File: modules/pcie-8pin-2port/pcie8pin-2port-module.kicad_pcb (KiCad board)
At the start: 4 copper layers, 109.7 x 66 mm, 24 parts, among them J1 TO-HUB, J5 USB-C 2.0, SW1 BOOT, SW2 RESET, U1 ESP32-S3-MINI-1-N4R2, U10 INA238, U11 INA238, U2 TJA1462A, U3 LP5907MFX-3.3

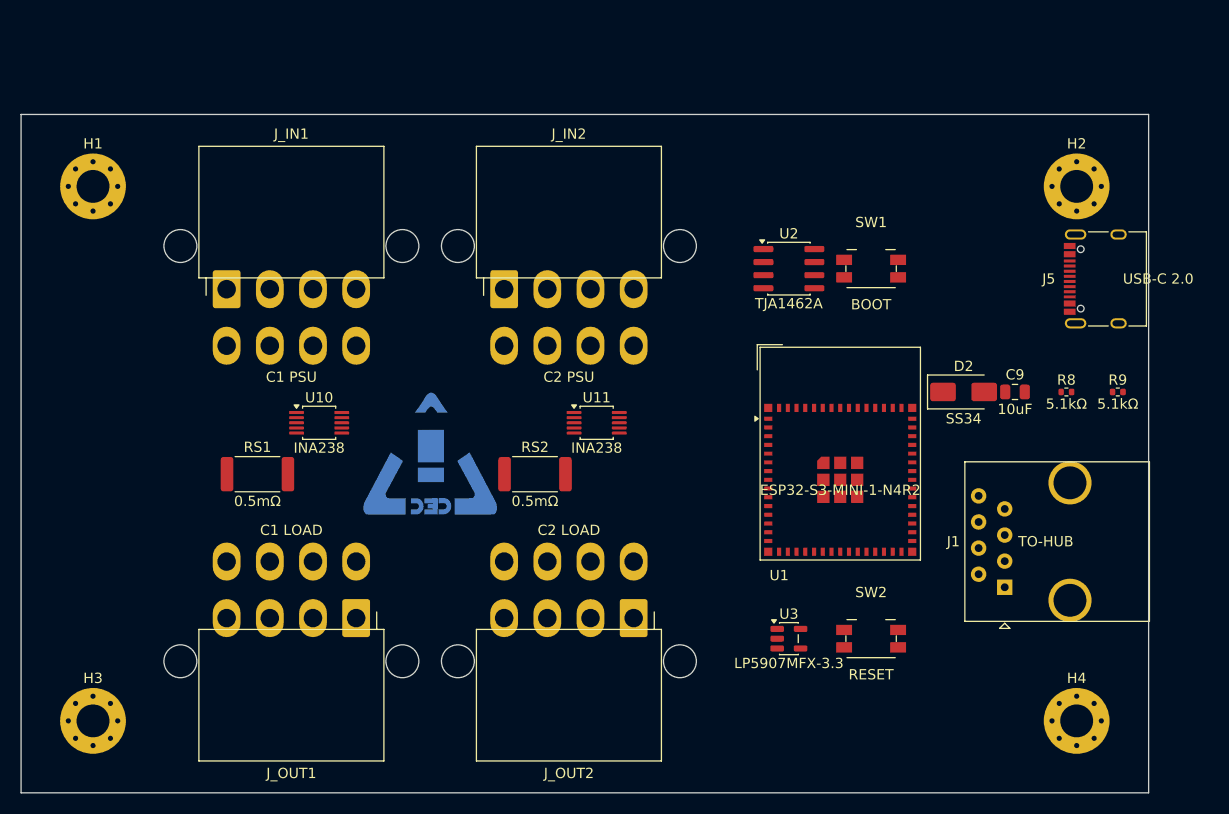
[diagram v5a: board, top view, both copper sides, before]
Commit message: pcie-2/3 PCB: condense + FTP jack (match the EPS pass)
Applied the same minimal-size / max-aggression pass to both PCIe SKUs, plus the
platform FTP jack swap.

- J1 RJ-45 -> platform FTP jack on both: footprint cec:RJ45_FTP_Shielded_Horizontal
  (Kinghelm KH-RJ45-58-8P8C, LCSC C2683360), SH1/SH2 -> GND (verbatim shield-tie
  splice; both PCIe J1 are at the same schematic position as the EPS/12VHPWR).
  Surgical edit (preserves the hand-applied sourcing); ERC benign-only, netlist
  verifies SH1/SH2 on GND + the FTP footprint. BOM CSVs J1 -> C2683360.
- Condensed PCB floorplans regenerated:
  - pcie-2port: 99 x 44 mm (identical geometry to the EPS, N=2): connectors
    overhang the edges, side-by-side sense band, RJ-45 mouth overhangs, USB-C on
    the top edge, 3 M3 mounts.
  - pcie-3port: 126 x 44 mm (N=3): same, but 5 M3 mounts -- the 3 base + two
    mid-height mounts in the inter-cable gaps so the long board doesn't flex (the
    overhang fills the top/bottom edges, leaving only the mid-height gaps free).
- gen-module-pcb.py: add inter-cable mid-height mounts for N>=3 cable boards.
- DRC 0 structural on both (only cosmetic silk + the benign lib_footprint_mismatch);
  renders confirm the FTP jack + the layout. PCBs still need GUI
  Update-from-Schematic + Fill Zones + route.

https://claude.ai/code/session_018vzBBqght166NSh7aJGKHf
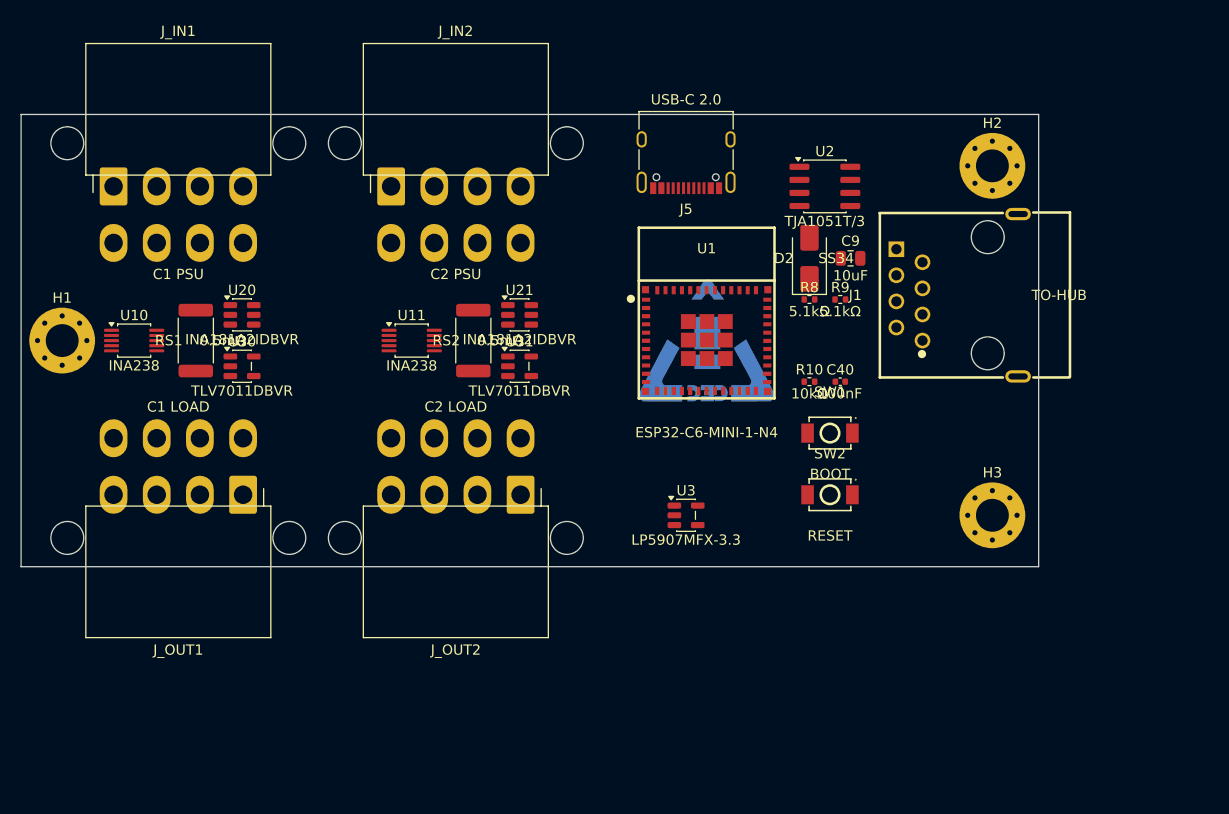
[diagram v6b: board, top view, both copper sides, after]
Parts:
- removed H4: MountingHole_3.2mm_M3_Pad_Via, cec-MountingHole:MountingHole_3.2mm_M3_Pad_Via
- added C40: 100nF, cec-Capacitor_SMD:C_0402_1005Metric, F.Cu at (79.7, 26.0)
- added R10: 10kΩ, cec-Resistor_SMD:R_0402_1005Metric, F.Cu at (76.7, 26.0)
- added U20: INA181A2IDBVR, cec-Package_TO_SOT_SMD:SOT-23-6, F.Cu at (21.5, 19.5)
- added U21: INA181A2IDBVR, cec-Package_TO_SOT_SMD:SOT-23-6, F.Cu at (48.5, 19.5)
- added U30: TLV7011DBVR, cec-Package_TO_SOT_SMD:SOT-23-5, F.Cu at (21.5, 24.5)
- added U31: TLV7011DBVR, cec-Package_TO_SOT_SMD:SOT-23-5, F.Cu at (48.5, 24.5)
- J1: footprint cec-Connector_RJ:RJ45_Amphenol_54602-x08_Horizontal -> cec:RJ45_FTP_Shielded_Horizontal
- SW1, SW2: footprint cec-Button_Switch_SMD:Panasonic_EVQPUJ_EVQPUA -> cec-Button_Switch_SMD:TS-1088-AR02016
- U1: value ESP32-S3-MINI-1-N4R2 -> ESP32-C6-MINI-1-N4; footprint cec-RF_Module:ESP32-S2-MINI-1_NoAntKeepout -> cec-RF_Module:ESP32-C6-MINI-1
- U2: value TJA1462A -> TJA1051T/3
- moved H3 89.8 mm to (94.5, 39.0)
- moved J5 42.9 mm to (64.7, 3.50), turned to 180 degrees
- moved LOGO1 29.1 mm to (66.7, 22.0)
- moved R9 28.5 mm to (79.7, 18.0)
- moved R8 26.6 mm to (76.7, 18.0)
- moved J1 25.3 mm to (87.7, 22.0)
- moved C9 20.6 mm to (80.7, 14.0)
- moved D2 19.8 mm to (76.7, 14.0), turned to 90 degrees
- moved U10 19.7 mm to (11.0, 22.0)
- moved U11 19.7 mm to (38.0, 22.0)
- moved U1 17.0 mm to (66.7, 22.0)
- moved SW1 16.5 mm to (78.7, 31.0)
- moved J_OUT1 16.3 mm to (21.6, 37.0)
- moved J_OUT2 16.3 mm to (48.6, 37.0)
- moved U3 15.6 mm to (64.7, 39.0)
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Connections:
- J1 pad SH1: unconnected-(J1-SHIELD-PadSH1) -> GND
- J1 pad SH2: unconnected-(J1-SHIELD-PadSH2) -> GND
- U1 pad 11: unconnected-(U1-IO7-Pad11) -> GND
- U1 pad 12: /I2C_SDA -> /DETECT_SENSE
- U1 pad 13: /I2C_SCL -> unconnected-(U1-IO1-Pad13)
- U1 pad 14: /DETECT_SENSE -> GND
- U1 pad 17: unconnected-(U1-IO13-Pad17) -> /USB_DM
- U1 pad 18: unconnected-(U1-IO14-Pad18) -> /USB_DP
- U1 pad 19: unconnected-(U1-IO15-Pad19) -> /THRESH_PWM
- U1 pad 21: /CAN_TX -> unconnected-(U1-NC-Pad21)
- U1 pad 22: /CAN_RX -> unconnected-(U1-IO8-Pad22)
- U1 pad 23: /USB_DM -> /GPIO0
- U1 pad 24: /USB_DP -> /I2C_SDA
- U1 pad 25: unconnected-(U1-IO21-Pad25) -> /I2C_SCL
- U1 pad 26: unconnected-(U1-IO26-Pad26) -> /CAN_TX
- U1 pad 27: unconnected-(U1-IO47-Pad27) -> /CAN_RX
- U1 pad 28: unconnected-(U1-IO33-Pad28) -> /DETC1
- U1 pad 29: unconnected-(U1-IO34-Pad29) -> /DETC2
- U1 pad 36: unconnected-(U1-IO40-Pad36) -> GND
- U1 pad 37: unconnected-(U1-IO41-Pad37) -> GND
- U1 pad 38: unconnected-(U1-IO42-Pad38) -> GND
- U1 pad 39: unconnected-(U1-TXD0-Pad39) -> GND
- U1 pad 4: /GPIO0 -> unconnected-(U1-NC-Pad4)
- U1 pad 40: unconnected-(U1-RXD0-Pad40) -> GND
- U1 pad 41: unconnected-(U1-IO45-Pad41) -> GND
- U1 pad 44: unconnected-(U1-IO46-Pad44) -> GND
- U1 pad 45: /EN -> GND
- U1 pad 8: unconnected-(U1-IO4-Pad8) -> /EN
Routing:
- added copper zone on In1.Cu, net GND
- added copper zone on In2.Cu, net GND
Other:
- board size 109.7 x 66 mm -> 99 x 44 mm

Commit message: Mini-Fit Jr footprint: correct pegs to the real Molex 5569-08A2 land
Verified the right-angle Mini-Fit Jr footprint against the actual Molex 5569-08A2
(KiCad-standard land / real drawing). The cec-derived land (made by trimming the
2x12 variant) had its two SNAP-IN PCB-lock pegs WRONG:

  was:  pegs (-4.5,-4.2) and (17.1,-4.2), 3.2mm drill  (outboard at the body ends)
  real: pegs (0,-7.3) and (12.6,-7.3),  3.0mm NPTH      (in line with the outer pins)

Signal pads (8x 2.7x3.7, 1.8mm, y0/5.5) and the F.Fab body already matched.
Also narrowed the courtyard to the real (-3.2,-14.4)..(15.8,7.85).

The real pegs sit ~3 mm further forward than the wrong ones, so the overhang
placement had to move the connectors inboard: gen-module-pcb.py JIN_Y 7 -> 10
(pegs now land 1.2 mm off the edge, mouth still overhangs ~3.9 mm), and the cable
boards grew H 44 -> 46 (BAND_Y 22 -> 23) to keep the side-by-side sense band clear
of the deeper connector courtyards.

PCIe-2 (99x46) and PCIe-3 (126x46) regenerated; DRC 0 structural, render confirms
the pegs now sit in line with the pins, on-board. EPS PCB intentionally NOT
regenerated (being hand-edited) -- it still carries the old peg land; on its next
Update-Footprints-from-Library the J_IN/J_OUT must shift to JIN_Y=10 / H=46.

https://claude.ai/code/session_018vzBBqght166NSh7aJGKHf
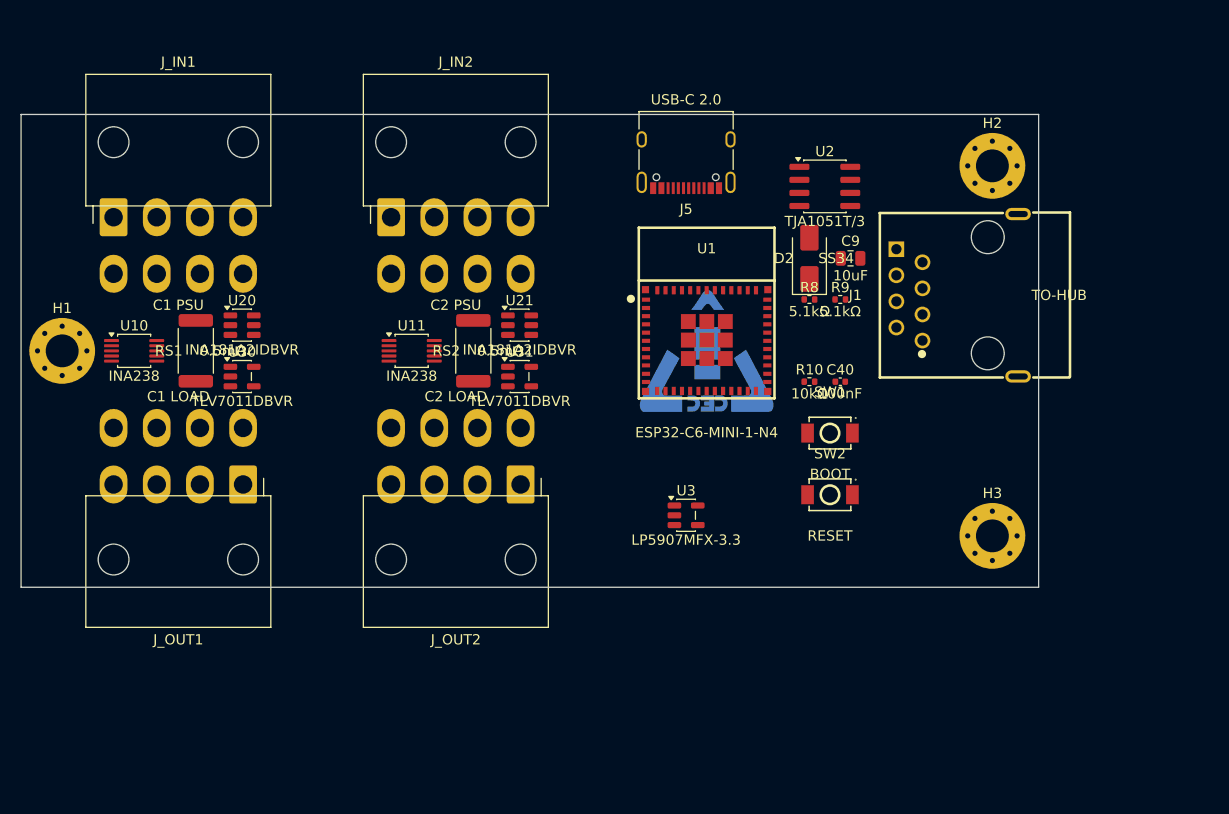
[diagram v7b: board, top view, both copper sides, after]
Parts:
- moved J_IN1 3.00 mm to (9.00, 10.0)
- moved J_IN2 3.00 mm to (36.0, 10.0)
- moved H3 2.00 mm to (94.5, 41.0)
- moved H1 1.00 mm to (4.00, 23.0)
- moved J_OUT1 1.00 mm to (21.6, 36.0)
- moved J_OUT2 1.00 mm to (48.6, 36.0)
- moved LOGO1 1.00 mm to (66.7, 23.0)
- moved RS1 1.00 mm to (17.0, 23.0)
- moved RS2 1.00 mm to (44.0, 23.0)
- moved U10 1.00 mm to (11.0, 23.0)
- moved U11 1.00 mm to (38.0, 23.0)
- moved U20 1.00 mm to (21.5, 20.5)
- moved U21 1.00 mm to (48.5, 20.5)
- moved U30 1.00 mm to (21.5, 25.5)
- moved U31 1.00 mm to (48.5, 25.5)
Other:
- board size 99 x 44 mm -> 99 x 46 mm

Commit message: pcie-2/3: adopt the REAL Molex 45586 cable connector (user-confirmed part)
The PCIe 8-pin header is Molex 45586-0005 (Mini-Fit Jr. dual-row right-angle,
3rd-gen PCIe polarization, 8 ckt, Nylon UL94V-0, 2.54um matte tin) — user
confirmed the keying and uploaded the Molex ECAD export. Adopt the manufacturer
land + STEP and retire the wrong cec-derived 5569 approximation for PCIe.

- Vendored lib/vendor/Connector_Molex.pretty/Molex_Mini-Fit_Jr_45586_2x04_
  P4.20mm_Horizontal.kicad_mod (Molex -SD export, kicad-cli fp upgrade to
  KiCad-10) + lib/3dmodels/Connector_Molex.3dshapes/<same>.step.
- Real land vs the prior 5569 approximation: 4.20mm pitch + **4.20mm ROWS**
  (not 5.5mm — the KiCad 5569 RA row spacing is a known-wrong footprint), round
  2.36mm / 1.85mm-drill pads, two 3.0mm snap pegs in line with the outer pins.
- Footprint is native mouth-toward-+y, so the generator now places J_IN rot180 /
  J_OUT rot0 (swapped). Verified this reproduces the exact same pad x-columns +
  numbering as before -> net map + 12V column alignment unchanged. gen-modules.py
  footprint_for(CEC_CONN_2x4) -> the 45586 land.
- PCIe-2/3 schematics repointed; J_IN/J_OUT sourced (Manufacturer=Molex,
  MPN=45586-0005; THT, consigned). BOM CSVs updated.
- The compact 45586 land (4.2mm rows + shallow courtyard) let the boards go back
  to 44 mm tall: 99x44 (PCIe-2) / 126x44 (PCIe-3). DRC 0 structural; pads+pegs
  verified on-board; renders confirm pegs in line with the pins, bodies overhang.

EPS NOT touched (being hand-edited) — still on the old 5569 land; it must move to
the same 45586 land (EPS12V-keyed MPN) with J_IN rot180/J_OUT rot0 + H=44 next.

https://claude.ai/code/session_018vzBBqght166NSh7aJGKHf
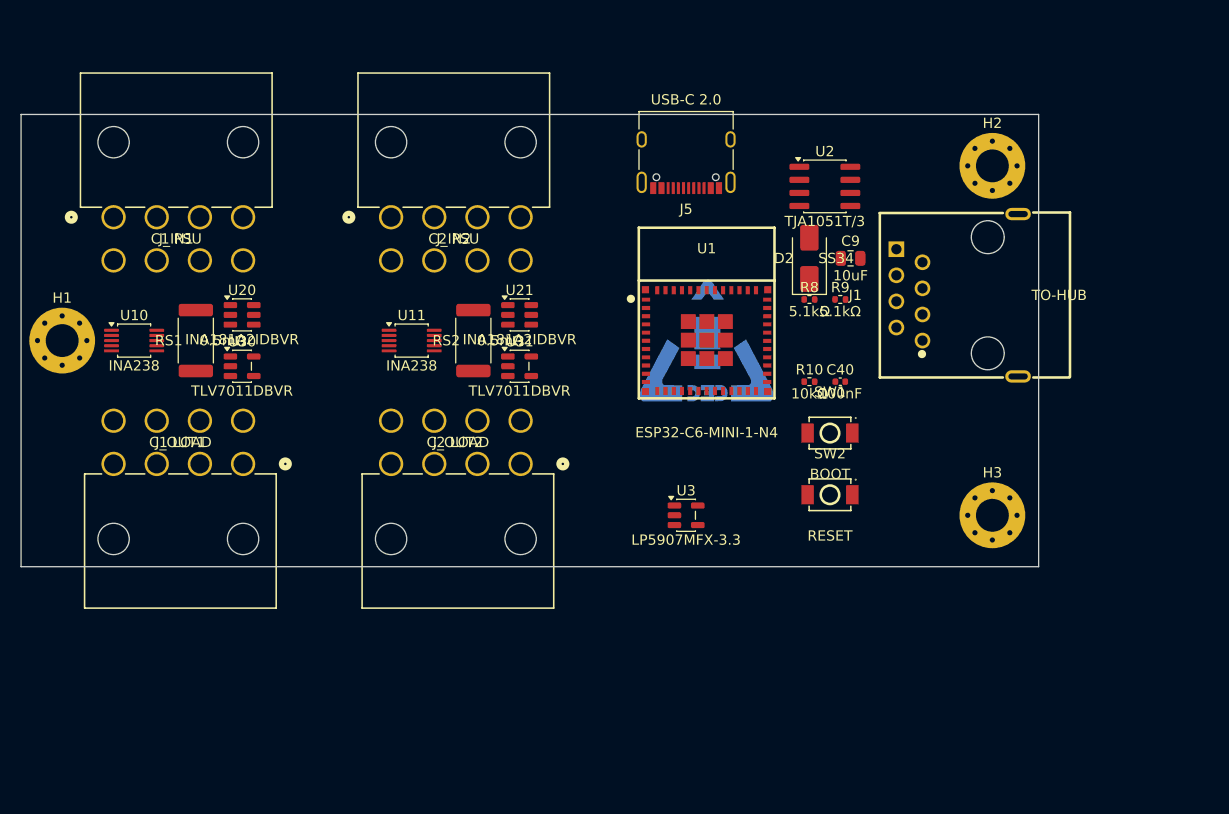
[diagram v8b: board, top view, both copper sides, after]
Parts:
- J_IN1, J_IN2, J_OUT1, J_OUT2: footprint cec-Connector_Molex:Molex_Mini-Fit_Jr_5569-08A2_2x04_P4.20mm_Horizontal -> cec-Connector_Molex:Molex_Mini-Fit_Jr_45586_2x04_P4.20mm_Horizontal
- moved H3 2.00 mm to (94.5, 39.0)
- moved J_OUT1 2.00 mm to (21.6, 34.0), turned to 0 degrees
- moved J_OUT2 2.00 mm to (48.6, 34.0), turned to 0 degrees
- moved H1 1.00 mm to (4.00, 22.0)
- moved LOGO1 1.00 mm to (66.7, 22.0)
- moved RS1 1.00 mm to (17.0, 22.0)
- moved RS2 1.00 mm to (44.0, 22.0)
- moved U10 1.00 mm to (11.0, 22.0)
- moved U11 1.00 mm to (38.0, 22.0)
- moved U20 1.00 mm to (21.5, 19.5)
- moved U21 1.00 mm to (48.5, 19.5)
- moved U30 1.00 mm to (21.5, 24.5)
- moved U31 1.00 mm to (48.5, 24.5)
- turned J_IN1 to 180 degrees
- turned J_IN2 to 180 degrees
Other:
- board size 99 x 46 mm -> 99 x 44 mm
